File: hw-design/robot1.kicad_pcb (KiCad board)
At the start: 2 copper layers, 63.5 x 26.7 mm, 78 parts, among them P1 test-double, P2 CONN_01X04, P3 CONN_01X03, P4 left_motor, P5 right_motor, P6 CONN_01X05, P7 CONN_01X05, P8 CONN_01X01, P9 CONN_01X01, U1 STM32F072CB/F042C6, U2 usb-micro, U3 MCP73833, U4 AP111733, U5 drv8835, U6 drv8835, U7 BlueNRG, U8 BALF-NRG-01D3, Y1 16MHz, Y2 32kHz, Y3 16MHz

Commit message: Gerbery 1.1
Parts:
- removed P8, P9: CONN_01X01, Mounting_Holes:MountingHole_2.2mm_M2_ISO7380
- added P10: CONN_01X02, w_pin_strip:pin_strip_2, F.Cu at (149.9, 128.9)
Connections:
- P3 pad 1: +BATT -> Net-(P10-Pad2)
- U3 pad 10: +BATT -> Net-(P10-Pad2)
- U3 pad 9: +BATT -> Net-(P10-Pad2)
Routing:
- net Net-(P10-Pad2): track 0.00 -> 16.9 mm, vias 0 -> 1
- net +BATT: track 85.0 -> 75.7 mm, vias 6 -> 4
- net GND: track 436.4 -> 441.8 mm
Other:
- board text added: "1.1"
- board text added: "Dla Frania"
- board text added: "straszne działo laserowo-radiowe (antena BT)"
- board text removed: "dla Frania"

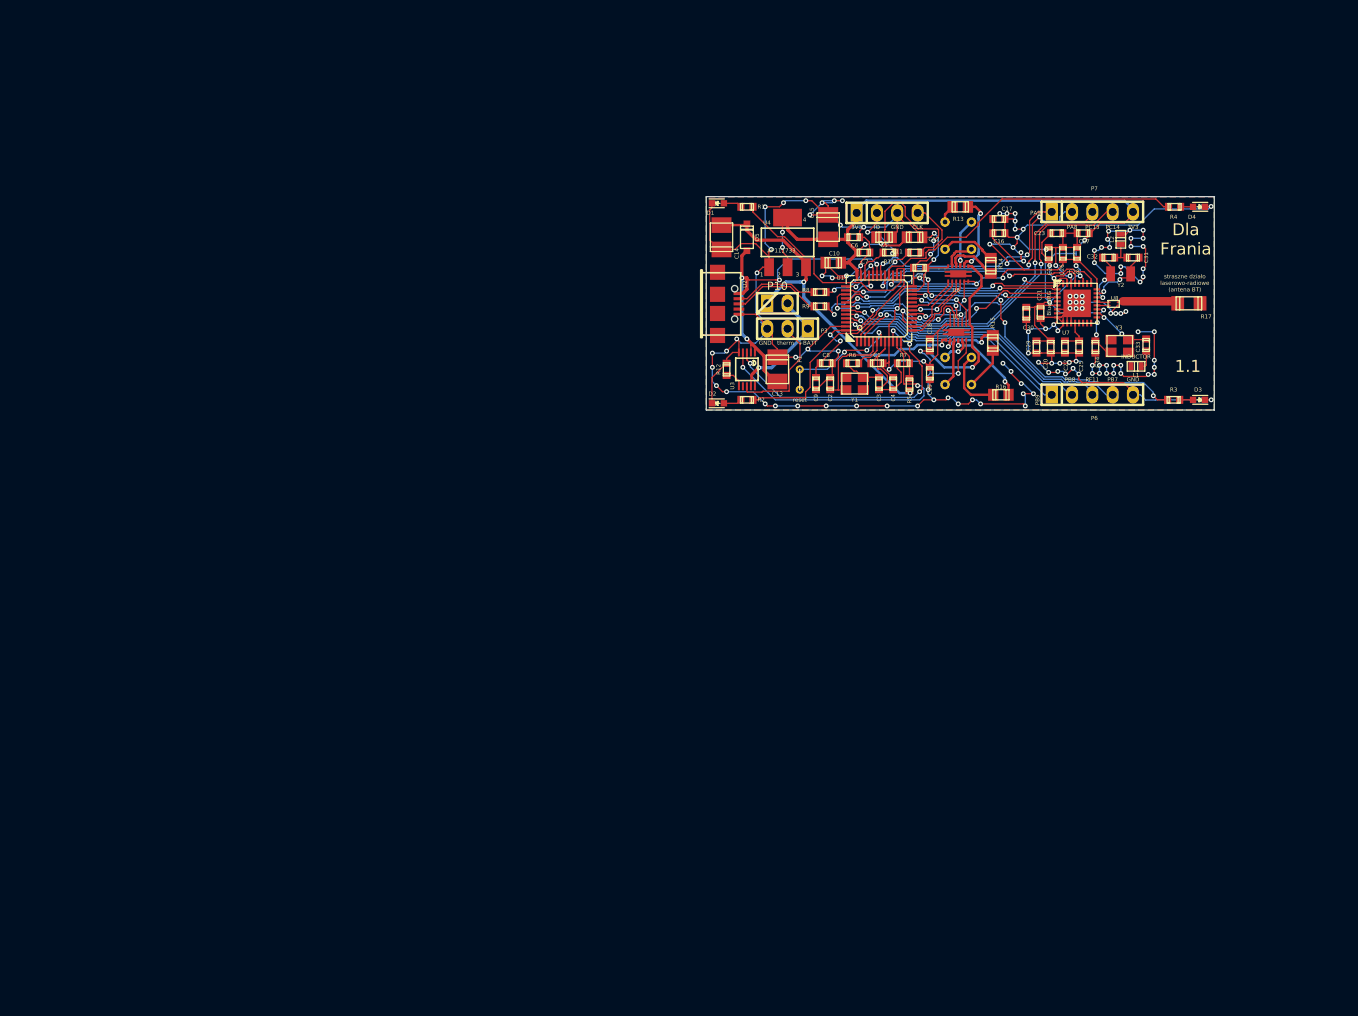
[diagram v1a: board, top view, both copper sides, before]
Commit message: 3 boards split
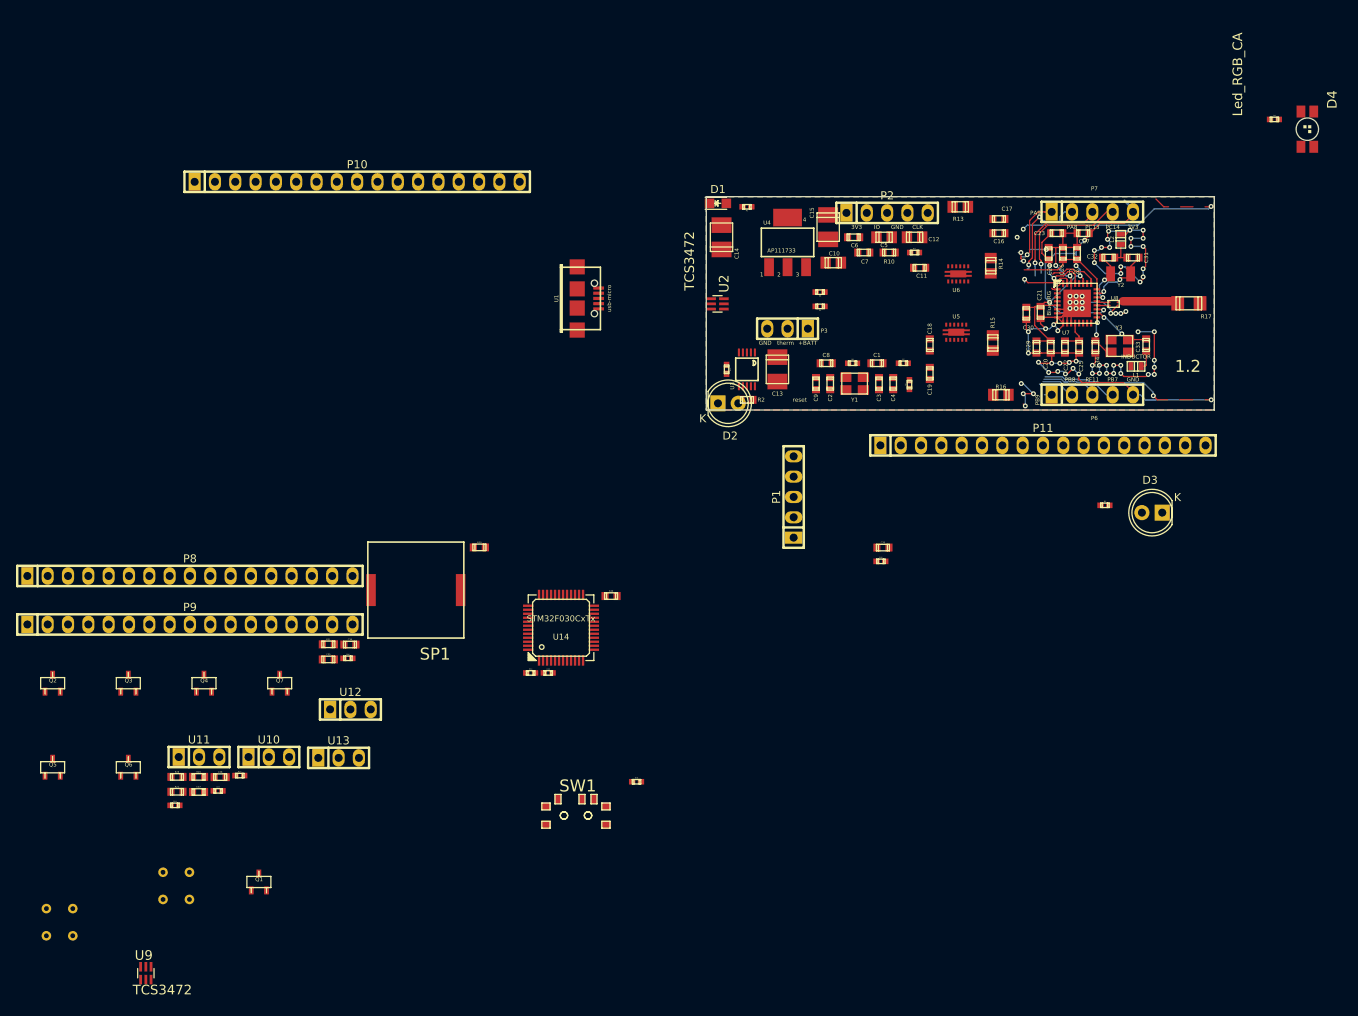
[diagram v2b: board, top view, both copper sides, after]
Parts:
- removed D5: D_Schottky, iwasz:sod123-pins21
- added C35: 100nF, w_smd_cap:c_0603, F.Cu at (93.7, 173.4)
- added C36: 100nF, w_smd_cap:c_0603, F.Cu at (96.4, 171.6)
- added C37: 100nF, w_smd_cap:c_0603, F.Cu at (77.5, 190.0)
- added C38: 100nF, w_smd_cap:c_0603, F.Cu at (80.2, 188.1)
- added C39: 15pF, w_smd_cap:c_0603, F.Cu at (163.0, 159.4)
- added C40: 15pF, w_smd_cap:c_0603, F.Cu at (129.1, 165.5)
- added P11: CONN_01X17, w_pin_strip:pin_strip_17, F.Cu at (183.1, 146.7)
- added P8: CONN_01X17, w_pin_strip:pin_strip_17, F.Cu at (76.4, 163.0)
- added P9: CONN_01X17, w_pin_strip:pin_strip_17, F.Cu at (76.4, 169.0)
- added Q1: BC847, w_smd_trans:sot23, F.Cu at (85.0, 201.2)
- added Q2: BC847, w_smd_trans:sot23, F.Cu at (59.3, 176.4)
- added Q3: BC847, w_smd_trans:sot23, F.Cu at (68.7, 176.4)
- added Q4: BC847, w_smd_trans:sot23, F.Cu at (78.2, 176.4)
- added Q5: BC847, w_smd_trans:sot23, F.Cu at (59.3, 186.9)
- added Q6: BC847, w_smd_trans:sot23, F.Cu at (68.7, 186.9)
- added Q7: BC847, w_smd_trans:sot23, F.Cu at (87.6, 176.4)
- added R18: 10k, w_smd_resistors:r_0402, F.Cu at (132.3, 188.7)
- added R21: 180R, w_smd_resistors:r_0603, F.Cu at (74.8, 190.0)
- added R24: 1k, w_smd_resistors:r_0402, F.Cu at (74.6, 191.7)
- added R25: 1k, w_smd_resistors:r_0402, F.Cu at (82.7, 187.9)
- added R26: 1k, w_smd_resistors:r_0402, F.Cu at (96.2, 173.3)
- added R27: 1k, w_smd_resistors:r_0402, F.Cu at (80.0, 189.8)
- added R28: 1k, w_smd_resistors:r_0603, F.Cu at (74.8, 188.1)
- added R29: 200, w_smd_resistors:r_0603, F.Cu at (77.5, 188.1)
- added R30: 30, w_smd_resistors:r_0603, F.Cu at (112.6, 159.4)
- added R31: 30, w_smd_resistors:r_0603, F.Cu at (93.7, 171.5)
- added R32: 22R, w_smd_resistors:r_0402, F.Cu at (162.8, 161.2)
- added R33: 22R, w_smd_resistors:r_0402, F.Cu at (119.0, 175.1)
- added R34: 220, w_smd_resistors:r_0402, F.Cu at (121.2, 175.1)
- added SP1: SPEAKER, iwasz:PKLCS-speaker, F.Cu at (105.1, 164.7)
- added SW1: SWITCH_INV, iwasz:1437575-1, F.Cu at (124.9, 192.7)
- added U10: China-0038, w_pin_strip:pin_strip_3, F.Cu at (86.3, 185.6)
- added U11: China-0038, w_pin_strip:pin_strip_3, F.Cu at (77.6, 185.6)
- added U12: China-0038, w_pin_strip:pin_strip_3, F.Cu at (96.5, 179.7)
- added U13: China-0038, w_pin_strip:pin_strip_3, F.Cu at (95.0, 185.7)
- added U14: STM32F030CxTx, w_smd_lqfp:lqfp48, F.Cu at (122.8, 169.5)
- added U9: TCS3472, iwasz:SC70-6, F.Cu at (70.9, 212.6)
- C2, C3: value ?10pF -> 100nF
- C31, C32: value 6pF -> 22pF
- C33, C34: value 10pF -> 15pF
- D1: footprint LEDs:LED_0603 -> LEDs:LED_0805
- D2: value LED -> VISHAY TLDR5800 (red 4°); footprint LEDs:LED_0603 -> LEDs:LED-5MM
- D3: value LED -> OSRAM SFH4550 (IR 3°); footprint LEDs:LED_0603 -> LEDs:LED-5MM
- D4: value LED -> Led_RGB_CA; footprint LEDs:LED_0603 -> iwasz:PLCC4-LED
- P1: value test-double -> CONN_01X05; footprint iwasz:testpad-2p -> w_pin_strip:pin_strip_5
- P10: value CONN_01X02 -> CONN_01X17; footprint w_pin_strip:pin_strip_2 -> w_pin_strip:pin_strip_17
- P2: value CONN_01X04 -> CONN_01X05; footprint w_pin_strip:pin_strip_4 -> w_pin_strip:pin_strip_5
- R1: value 680R -> 1k; footprint w_smd_resistors:r_0603 -> w_smd_resistors:r_0402
- R10: value 22R -> 130
- R11, R9: value 22R -> 1k; footprint w_smd_resistors:r_0603 -> w_smd_resistors:r_0402
- R12, R5, R7: footprint w_smd_resistors:r_0603 -> w_smd_resistors:r_0402
- R2: value 680R -> 80
- R3, R4: value 680R -> 1R; footprint w_smd_resistors:r_0603 -> w_smd_resistors:r_0402
- R6: value 220R -> 1R; footprint w_smd_resistors:r_0603 -> w_smd_resistors:r_0402
- R8: value 22R -> 1R; footprint w_smd_resistors:r_0603 -> w_smd_resistors:r_0402
- U1: value STM32F072CB/F042C6 -> usb-micro; footprint w_smd_lqfp:lqfp48 -> w_conn_pc:conn_usb_B_micro_smd-2
- U2: value usb-micro -> TCS3472; footprint w_conn_pc:conn_usb_B_micro_smd-2 -> iwasz:SC70-6
- moved P4 141.4 mm to (63.1, 200.9)
- moved P5 117.0 mm to (71.7, 207.1)
- moved P10 54.7 mm to (97.3, 113.7)
- moved U1 37.7 mm to (124.8, 128.3), turned to 270 degrees
- moved D4 16.7 mm to (216.1, 107.1)
- moved R4 16.6 mm to (212.0, 105.9)
- moved R3 15.7 mm to (190.8, 154.2)
- moved D3 14.8 mm to (198.0, 155.1)
- moved P1 14.7 mm to (151.9, 153.1)
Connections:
- C2 pad 1: Net-(C2-Pad1) -> GND
- C2 pad 2: GND -> +3V3
- C3 pad 1: Net-(C3-Pad1) -> GND
- C3 pad 2: GND -> +3V3
- D1 pad 1: GND -> Net-(D1-Pad1)
- D2 pad 1: GND -> Net-(D2-Pad1)
- D3 pad 1: GND -> Net-(D3-Pad1)
- D4 pad 1: GND -> +3V3
- P1 pad 1: Net-(P1-Pad1) -> /micro/aphasel
- P10 pad 1: +BATT -> /micro/aphasel
- P10 pad 2: Net-(P10-Pad2) -> /micro/bphasel
- P2 pad 1: +3V3 -> Net-(P2-Pad1)
- P2 pad 2: Net-(P2-Pad2) -> +3V3
- P2 pad 3: GND -> Net-(P2-Pad3)
- P2 pad 4: Net-(P2-Pad4) -> GND
- P3 pad 1: Net-(P10-Pad2) -> Net-(P3-Pad1)
- P6 pad 1: Net-(P6-Pad1) -> +5V
- P6 pad 2: Net-(P6-Pad2) -> /micro/benblr
- P6 pad 3: Net-(P6-Pad3) -> /micro/aenblr
- P6 pad 4: Net-(P6-Pad4) -> /micro/bphaser
- P6 pad 5: GND -> /micro/aphaser
- P7 pad 1: Net-(P7-Pad1) -> /micro/photo_illumination
- P7 pad 2: Net-(P7-Pad2) -> /micro/photo_l_int
- P7 pad 3: /micro/head1 -> /micro/photo_r_int
- P7 pad 4: /micro/head2 -> /micro/scl
- P7 pad 5: +3V3 -> /micro/sda
- R1 pad 1: Net-(D1-Pad2) -> Net-(Q1-Pad2)
- R1 pad 2: /micro/led1 -> /micro/photo_illumination
- R10 pad 1: Net-(P2-Pad2) -> Net-(D2-Pad2)
- R10 pad 2: /micro/swdio -> +3V3
- R11 pad 1: Net-(P2-Pad4) -> Net-(Q3-Pad2)
- R11 pad 2: /micro/swdclk -> /micro/ir_cannon
- R2 pad 1: Net-(D2-Pad2) -> Net-(D1-Pad2)
- R2 pad 2: /micro/led2 -> +BATT
- R3 pad 1: Net-(D3-Pad2) -> +3V3
- R3 pad 2: /micro/led3 -> Net-(C36-Pad2)
- R4 pad 1: Net-(D4-Pad2) -> +3V3
- R4 pad 2: /micro/led4 -> Net-(C37-Pad2)
- R6 pad 1: Net-(R6-Pad1) -> +3V3
- R6 pad 2: Net-(C3-Pad1) -> Net-(C35-Pad2)
- R8 pad 1: Net-(R8-Pad1) -> +3V3
- R8 pad 2: Net-(R8-Pad2) -> Net-(C38-Pad2)
- R9 pad 1: Net-(R9-Pad1) -> Net-(Q2-Pad2)
- R9 pad 2: Net-(R9-Pad2) -> /micro/ir_cannon
- U1 pad 1: Net-(U1-Pad1) -> +5V
- U1 pad 2: /micro/head1 -> Net-(U1-Pad2)
- U1 pad 3: /micro/head2 -> Net-(U1-Pad3)
- U1 pad 5: Net-(C2-Pad1) -> GND
- U2 pad 1: +5V -> +3V3
- U2 pad 2: Net-(R8-Pad1) -> /micro/scl
- U2 pad 3: Net-(R9-Pad1) -> GND
- U2 pad 5: GND -> /micro/photo_l_int
- U3 pad 10: Net-(P10-Pad2) -> Net-(P3-Pad1)
- U3 pad 9: Net-(P10-Pad2) -> Net-(P3-Pad1)
- Y1 pad 1: Net-(C2-Pad1) -> Net-(C39-Pad1)
- Y1 pad 2: Net-(C3-Pad1) -> Net-(C40-Pad1)
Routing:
- net GND: track 441.8 -> 139.0 mm, vias 125 -> 64
- net +3V3: track 240.1 -> 61.5 mm, vias 22 -> 5
- net +BATT: track 75.7 -> 0.00 mm, vias 4 -> 0
- net (no net): track 0.00 -> 55.0 mm, vias 0 -> 10
- net /micro/led3: track 46.4 -> 0.00 mm, vias 6 -> 0
- net +5V: track 44.4 -> 0.91 mm, vias 4 -> 0
- net /micro/head2: track 43.0 -> 0.00 mm, vias 2 -> 0
- net /micro/head1: track 41.2 -> 0.00 mm, vias 2 -> 0
- net /micro/led4: track 40.3 -> 0.00 mm
- net Net-(P6-Pad4): track 38.2 -> 0.00 mm, vias 1 -> 0
- net /micro/progress: track 35.8 -> 0.00 mm, vias 4 -> 0
- net /micro/complete: track 35.7 -> 0.00 mm, vias 2 -> 0
- net Net-(P6-Pad3): track 35.5 -> 0.00 mm, vias 1 -> 0
- net Net-(P7-Pad2): track 33.2 -> 0.00 mm, vias 3 -> 0
- net Net-(P6-Pad2): track 32.6 -> 0.00 mm, vias 1 -> 0
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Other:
- board text added: "1.2"
- board text removed: "1.1"
- board text removed: "Dla Frania"
- board text removed: "straszne działo laserowo-radiowe (antena BT)"

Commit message: Another idea of PCB split.
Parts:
- removed P10, P11: CONN_01X17, w_pin_strip:pin_strip_17
- removed R32, R33: 22R, w_smd_resistors:r_0402
- added R19: 22R, w_smd_resistors:r_0402, F.Cu at (161.3, 138.6)
- added R20: 22R, w_smd_resistors:r_0402, F.Cu at (156.2, 138.6)
- C14, C15: value 10µF -> 1µF X7R 10V; footprint w_smd_cap:c_tant_B -> w_smd_cap:c_0603
- C16, C17, C18, C19, C2, C3, D1, Q1, R1, R18, R2, SW1, U1, U2, U9: moved to B.Cu
- P1, P2, P6, P7: value CONN_01X05 -> CONN_01X17; footprint w_pin_strip:pin_strip_5 -> iwasz:pin_socket_17
- P8, P9: footprint w_pin_strip:pin_strip_17 -> iwasz:pin_socket_17
- U4: value AP111733 -> MIC5501; footprint linear:SOT223 -> w_smd_trans:sot23-5
- moved D4 233.9 mm to (-9.27, 169.7)
- moved R4 187.3 mm to (38.3, 176.2)
- moved R3 153.5 mm to (37.8, 167.2)
- moved D3 140.5 mm to (57.9, 143.4)
- moved P5 140.4 mm to (179.7, 117.2), turned to 270 degrees
- moved R8 128.0 mm to (38.6, 180.3)
- moved R6 126.1 mm to (38.2, 171.7)
- moved P4 125.9 mm to (173.7, 140.6), turned to 90 degrees
- moved SP1 125.5 mm to (-16.6, 195.5)
- moved R30 119.5 mm to (-5.46, 177.5)
- moved R10 110.1 mm to (62.4, 165.4), turned to 90 degrees
- moved R11 108.5 mm to (61.5, 147.9)
- moved R26 108.3 mm to (-12.1, 176.5)
- moved R25 106.8 mm to (-22.9, 171.3)
- moved Q1 101.0 mm to (100.5, 101.4), turned to 270 degrees
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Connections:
- C35 pad 1: GND -> GNDA
- C36 pad 1: GND -> GNDA
- C37 pad 1: GND -> GNDA
- C38 pad 1: GND -> GNDA
- D4 pad 1: +3V3 -> +3.3VP
- P2 pad 1: Net-(P2-Pad1) -> /micro/photo_illumination
- P2 pad 2: +3V3 -> /micro/photo_l_int
- P2 pad 3: Net-(P2-Pad3) -> /micro/photo_r_int
- P2 pad 4: GND -> /micro/scl
- P2 pad 5: Net-(P2-Pad5) -> /micro/sda
- P6 pad 1: +5V -> Net-(P6-Pad1)
- P6 pad 2: /micro/benblr -> Net-(P6-Pad2)
- P6 pad 3: /micro/aenblr -> Net-(P6-Pad3)
- P6 pad 4: /micro/bphaser -> Net-(P6-Pad4)
- P6 pad 5: /micro/aphaser -> +BATT
- P7 pad 1: /micro/photo_illumination -> /photo/photo_illumination
- P7 pad 2: /micro/photo_l_int -> /photo/photo_l_int
- P7 pad 3: /micro/photo_r_int -> /photo/photo_r_int
- P7 pad 4: /micro/scl -> /photo/scl
- P7 pad 5: /micro/sda -> /photo/sda
- P8 pad 10: /micro/ir_sense -> /peripherals/ir_sense
- P8 pad 14: +3V3 -> +3.3VP
- P8 pad 16: GND -> GNDA
- P8 pad 5: +BATT -> VAA
- P8 pad 6: /micro/led_b -> /peripherals/led_b
- P8 pad 7: /micro/led_g -> /peripherals/led_g
- P8 pad 8: /micro/led_r -> /peripherals/led_r
- P8 pad 9: /micro/ir_cannon -> /peripherals/ir_cannon
- P9 pad 13: +5V -> Net-(P9-Pad13)
- P9 pad 6: GND -> GNDA
- P9 pad 7: /micro/sound -> /peripherals/sound
- Q2 pad 3: GND -> GNDA
- Q3 pad 3: GND -> GNDA
- Q4 pad 3: GND -> GNDA
- Q5 pad 3: GND -> GNDA
- Q6 pad 3: GND -> GNDA
- Q7 pad 3: GND -> GNDA
- R1 pad 2: /micro/photo_illumination -> /photo/photo_illumination
- R10 pad 2: +3V3 -> +3.3VP
- R11 pad 2: /micro/ir_cannon -> /peripherals/ir_cannon
- R21 pad 2: +3V3 -> +3.3VP
- R24 pad 2: /micro/sound -> /peripherals/sound
- R25 pad 2: /micro/led_r -> /peripherals/led_r
- R26 pad 2: /micro/led_g -> /peripherals/led_g
- R27 pad 2: /micro/led_b -> /peripherals/led_b
- R28 pad 2: +BATT -> VAA
- R3 pad 1: +3V3 -> +3.3VP
- R4 pad 1: +3V3 -> +3.3VP
- R6 pad 1: +3V3 -> +3.3VP
- R8 pad 1: +3V3 -> +3.3VP
- R9 pad 2: /micro/ir_cannon -> /peripherals/ir_cannon
- SP1 pad 1: +BATT -> VAA
- U10 pad 1: /micro/ir_sense -> /peripherals/ir_sense
- U10 pad 2: GND -> GNDA
- U11 pad 1: /micro/ir_sense -> /peripherals/ir_sense
- U11 pad 2: GND -> GNDA
- U12 pad 1: /micro/ir_sense -> /peripherals/ir_sense
- U12 pad 2: GND -> GNDA
- U13 pad 1: /micro/ir_sense -> /peripherals/ir_sense
- U13 pad 2: GND -> GNDA
- U2 pad 2: /micro/scl -> /photo/scl
- U2 pad 5: /micro/photo_l_int -> /photo/photo_l_int
- U2 pad 6: /micro/sda -> /photo/sda
- U4 pad 1: GND -> +3V3
- U4 pad 2: +3V3 -> GND
- U4 pad 3: +BATT -> Net-(U4-Pad3)
- U4 pad 4: +3V3 -> +BATT
- U9 pad 2: /micro/scl -> /photo/scl
- U9 pad 5: /micro/photo_r_int -> /photo/photo_r_int
- U9 pad 6: /micro/sda -> /photo/sda
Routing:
- net +BATT: track 0.00 -> 73.4 mm, vias 0 -> 3
- net +3V3: track 61.5 -> 133.2 mm, vias 5 -> 14
- net /micro/aenbll: track 0.00 -> 55.3 mm, vias 0 -> 2
- net (no net): track 55.0 -> 0.00 mm, vias 10 -> 0
- net +5V: track 0.91 -> 47.4 mm, vias 0 -> 1
- net /micro/benbll: track 0.00 -> 45.0 mm, vias 0 -> 2
- net /micro/bphasel: track 0.00 -> 44.8 mm, vias 0 -> 5
- net /micro/aphasel: track 0.00 -> 42.5 mm, vias 0 -> 2
- net /micro/aenblr: track 7.08 -> 46.4 mm, vias 0 -> 2
- net GND: track 139.0 -> 177.2 mm
- net /micro/bphaser: track 9.42 -> 46.2 mm, vias 0 -> 2
- net /micro/aphaser: track 12.9 -> 48.5 mm, vias 1 -> 2
- net /micro/benblr: track 4.62 -> 38.9 mm, vias 0 -> 2
- net /micro/pc13: track 0.00 -> 29.3 mm, vias 0 -> 1
- net /micro/pc14: track 0.00 -> 28.3 mm, vias 0 -> 1
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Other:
- board size 63.5 x 26.7 mm -> 49.7 x 26.7 mm
- net class Default: via_dia 0.6096 -> 0.4572; via_drill 0.3048 -> 0.1524
- rule via_min_drill: 0.3048 -> 0.1524
- rule via_min_size: 0.6096 -> 0.4572
- board text added: "franek"
- board text added: "iwasz"
